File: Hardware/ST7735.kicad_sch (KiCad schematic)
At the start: 9 parts

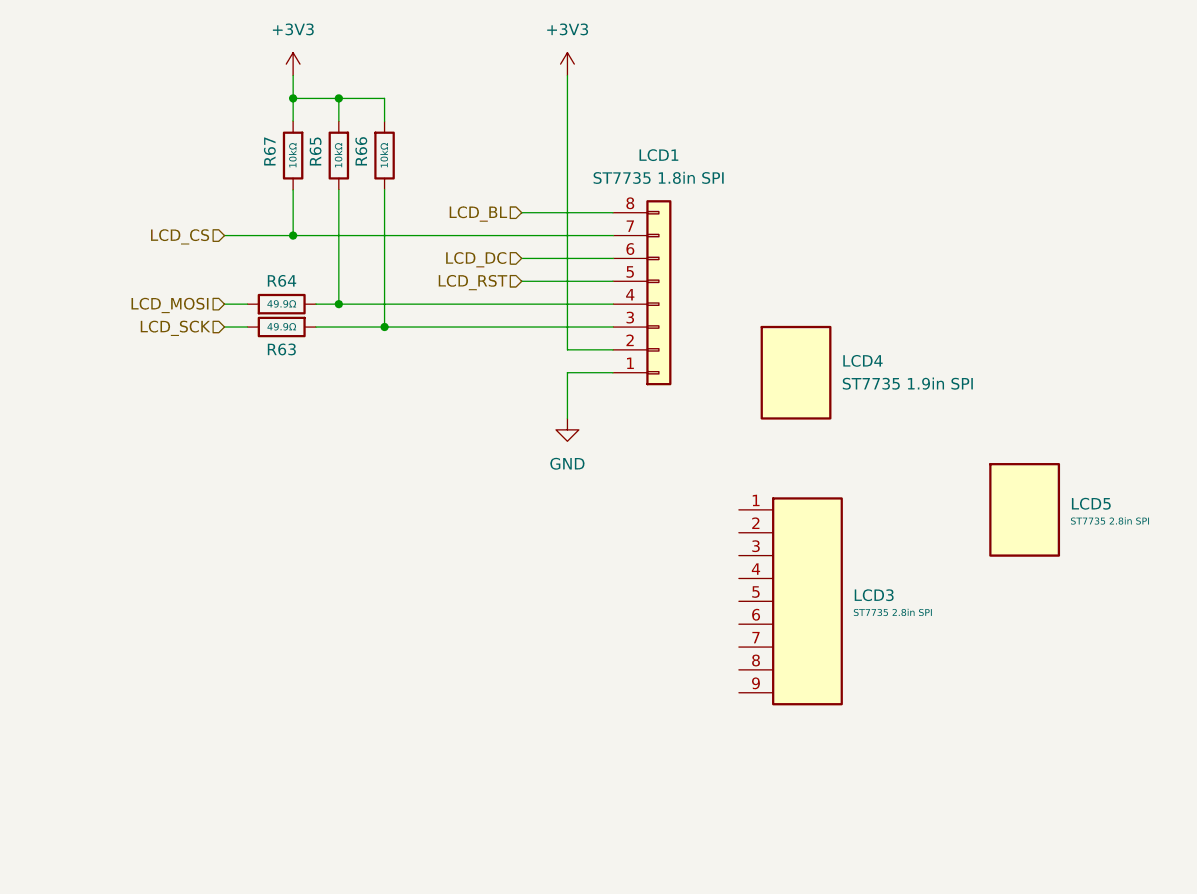
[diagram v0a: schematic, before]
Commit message: remove unused sheets
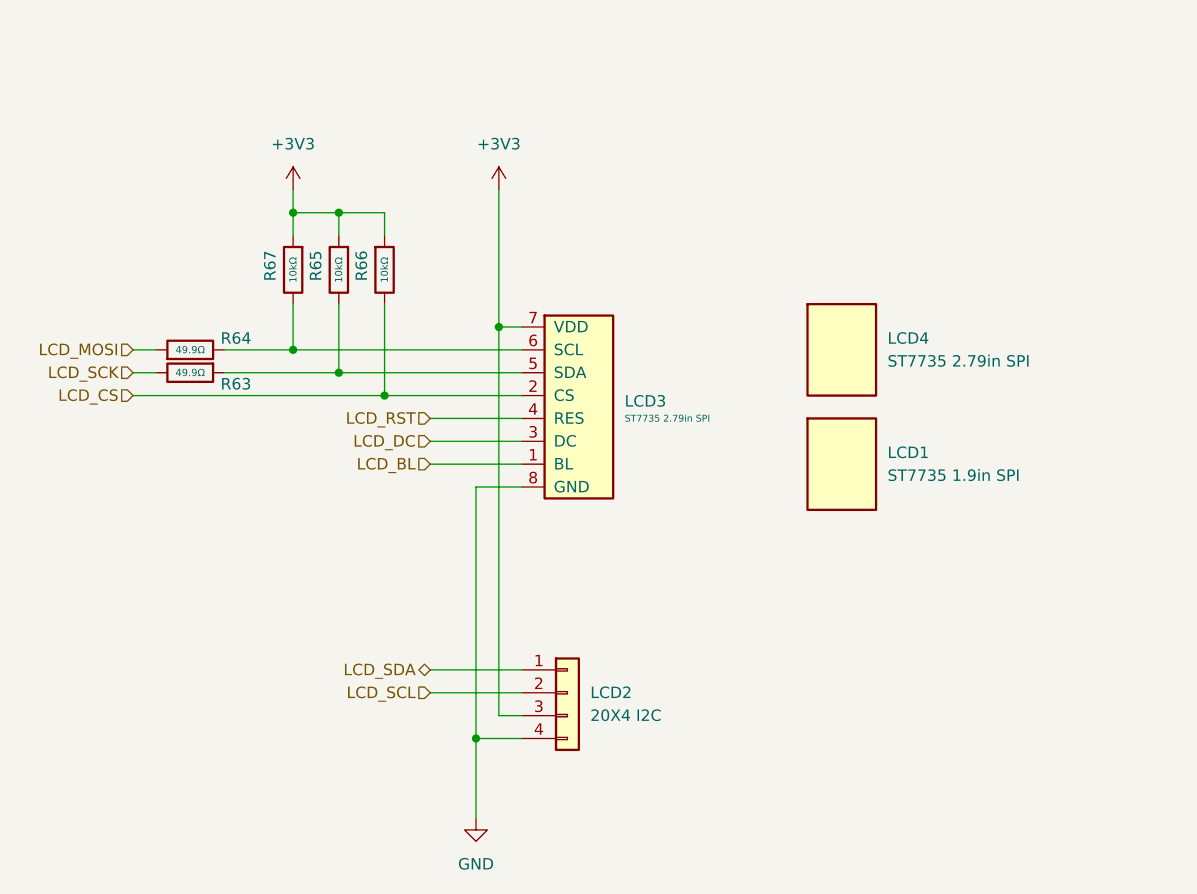
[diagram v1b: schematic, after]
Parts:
- removed LCD1: ST7735 1.8in SPI, EASYEDA2KICAD:LCD, ST7735 1.8in SPI, symbol PCM_JLCPCB-Extended:LCD, ST7735 1.8in SPI
- removed LCD3: ST7735 2.8in SPI, AderbTech:LCD 2.8 INCH SPI HEADER, symbol AderbTech:LCD, ST7735 2.8in SPI
- removed LCD4: ST7735 1.9in SPI, AderbTech:LCD 1.9 INCH SPI ST7735, symbol AderbTech:LCD, ST7735 SCREEN 1.9
- removed LCD5: ST7735 2.8in SPI, AderbTech:LCD 2.8 INCH SPI ST7735, symbol AderbTech:LCD, ST7735 SCREEN 2.8
- added LCD1: ST7735 1.9in SPI, AderbTech:LCD 1.8 INCH SPI ST7735, symbol AderbTech:LCD, ST7735 SCREEN 1.9
- added LCD2: 20X4 I2C, Connector_Molex:Molex_KK-254_AE-6410-04A_1x04_P2.54mm_Vertical, symbol Connector_Generic:Conn_01x04
- added LCD3: ST7735 2.79in SPI, AderbTech:LCD 2.79 INCH SPI HEADER NMH, symbol AderbTech:LCD, ST7735 2.79in SPI
- added LCD4: ST7735 2.79in SPI, AderbTech:LCD 2.79 INCH SPI ST7789, symbol AderbTech:LCD, ST7735 SCREEN 2.79
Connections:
- net +3V3: now also LCD2.3 (Pin_3), LCD3.7 (VDD)
- net GND: now also LCD2.4 (Pin_4), LCD3.8 (GND)
- net LCD_BL: now also LCD3.1 (BL)
- net LCD_CS: now also R66.2, LCD3.2 (CS); no longer R67.2
- net LCD_DC: now also LCD3.3 (DC)
- net LCD_RST: now also LCD3.4 (RES)
- net at R65.2: now also R63.1, LCD3.5 (SDA); no longer R64.2
- new net: LCD3.6 (SCL), R64.2, R67.2
- new net LCD_SCL: LCD2.2 (Pin_2)
- new net LCD_SDA: LCD2.1 (Pin_1)
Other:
- moved on the sheet: R63, R64, R65, R66, R67
